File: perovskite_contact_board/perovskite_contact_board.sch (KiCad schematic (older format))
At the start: 14 parts, among them J1 Conn_02x03_Counter_Clockwise, J2 Conn_02x03_Counter_Clockwise, J3 Conn_02x03_Counter_Clockwise, J4 Conn_02x03_Counter_Clockwise, J5 Conn_02x03_Counter_Clockwise, J6 Conn_02x03_Counter_Clockwise, U1 Perovskite_CP_6_Cell, U2 Perovskite_CP_6_Cell, U3 Perovskite_CP_6_Cell, U4 MCP9808_MSOP, U5 MCP9808_MSOP, U6 MCP9808_MSOP

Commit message: pushing changes from Monday meeting
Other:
- moved on the sheet: R1, R4, U1, U2, U3, U4, U5, U6

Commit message: Switched to 0603 package, no longer castillated holes used for the mcp9804, all traces on back layer
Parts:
- removed J1, J2, J3, J4, J5, J6: Conn_02x03_Counter_Clockwise, Connector_PinHeader_2.54mm:PinHeader_2x03_P2.54mm_Vertical_SMD, symbol Connector_Generic:Conn_02x03_Counter_Clockwise
- added J1, J2, J3, J4, J5, J6: Conn_01x08, Connector_PinSocket_2.54mm:PinSocket_1x08_P2.54mm_Vertical_SMD_Pin1Left, symbol Connector_Generic:Conn_01x08
- R1, R4: footprint Resistor_SMD:R_0805_2012Metric -> Resistor_SMD:R_0603_1608Metric
- U4, U5, U6: footprint MCP9804Castillated:CastillatedMCP9804 -> MCP9804_Custom:MCP9804_With_Hole
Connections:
- net labels added: +5V, ALERT1, ALERT2, ALERT3, CELL_1, CELL_10, CELL_11, CELL_12, CELL_13, CELL_14, CELL_15, CELL_16, CELL_17, CELL_18, CELL_2, CELL_3, CELL_4, CELL_5, CELL_6, CELL_7, CELL_8, CELL_9
- net labels removed: 1, 10, 11, 12, 13, 14, 15, 16, 17, 18, 2, 3, 4, 5, 6, 7, 8, 9, Alert1, Alert2, Alert3, Vdd
- wire segments 15 -> 73
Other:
- note added: "Perovskite 1"
- note added: "Perovskite 2"
- note added: "Perovskite 3"
- note added: "Pull Up"
- moved on the sheet: R1, R4, U1, U2, U3, U4, U5, U6

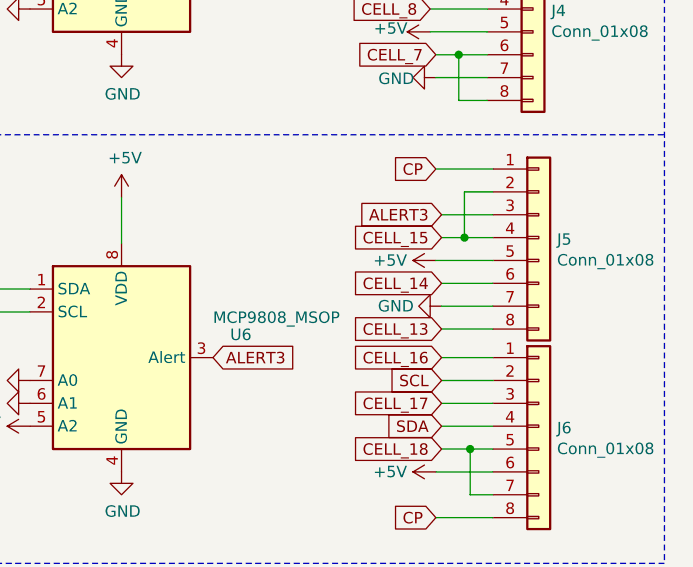
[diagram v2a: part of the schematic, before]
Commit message: Contact board update with 2.54 spacing
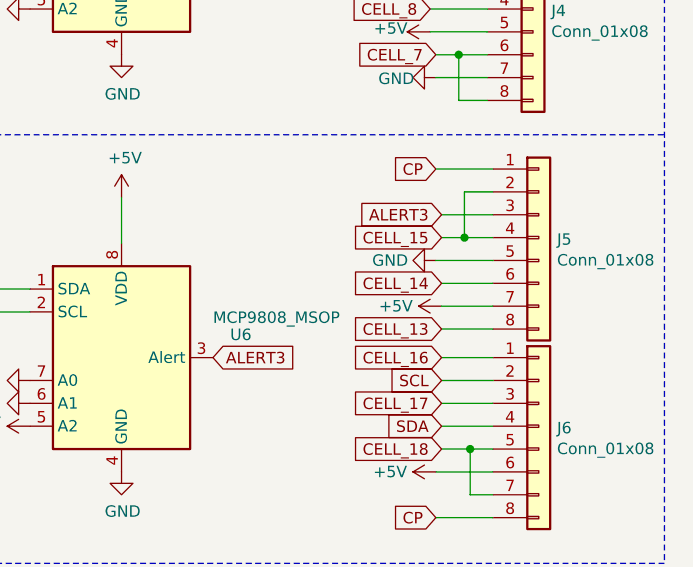
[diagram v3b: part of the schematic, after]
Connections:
- net +5V: now also J5.7 (Pin_7); no longer J5.5 (Pin_5)
- net GND: now also J5.5 (Pin_5); no longer J5.7 (Pin_7)
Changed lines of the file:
@@
 L power:GND #PWR0121
 U 1 1 636DD992
-P 7125 5175
-F 0 "#PWR0121" H 7125 4925 50  0001 C CNN
-F 1 "GND" V 7125 4975 50  0000 C CNN
-F 2 "" H 7125 5175 50  0001 C CNN
-F 3 "" H 7125 5175 50  0001 C CNN
-	1    7125 5175
+P 7100 4975
+F 0 "#PWR0121" H 7100 4725 50  0001 C CNN
+F 1 "GND" V 7100 4775 50  0000 C CNN
+F 2 "" H 7100 4975 50  0001 C CNN
+F 3 "" H 7100 4975 50  0001 C CNN
+	1    7100 4975
 	0    1    1    0
 $EndComp
@@
 L power:+5V #PWR0123
 U 1 1 6375EA4D
-P 7100 4975
-F 0 "#PWR0123" H 7100 4825 50  0001 C CNN
-F 1 "+5V" V 7100 5175 50  0000 C CNN
-F 2 "" H 7100 4975 50  0001 C CNN
-F 3 "" H 7100 4975 50  0001 C CNN
-	1    7100 4975
+P 7125 5175
+F 0 "#PWR0123" H 7125 5025 50  0001 C CNN
+F 1 "+5V" V 7125 5375 50  0000 C CNN
+F 2 "" H 7125 5175 50  0001 C CNN
+F 3 "" H 7125 5175 50  0001 C CNN
+	1    7125 5175
 	0    -1   1    0
 $EndComp

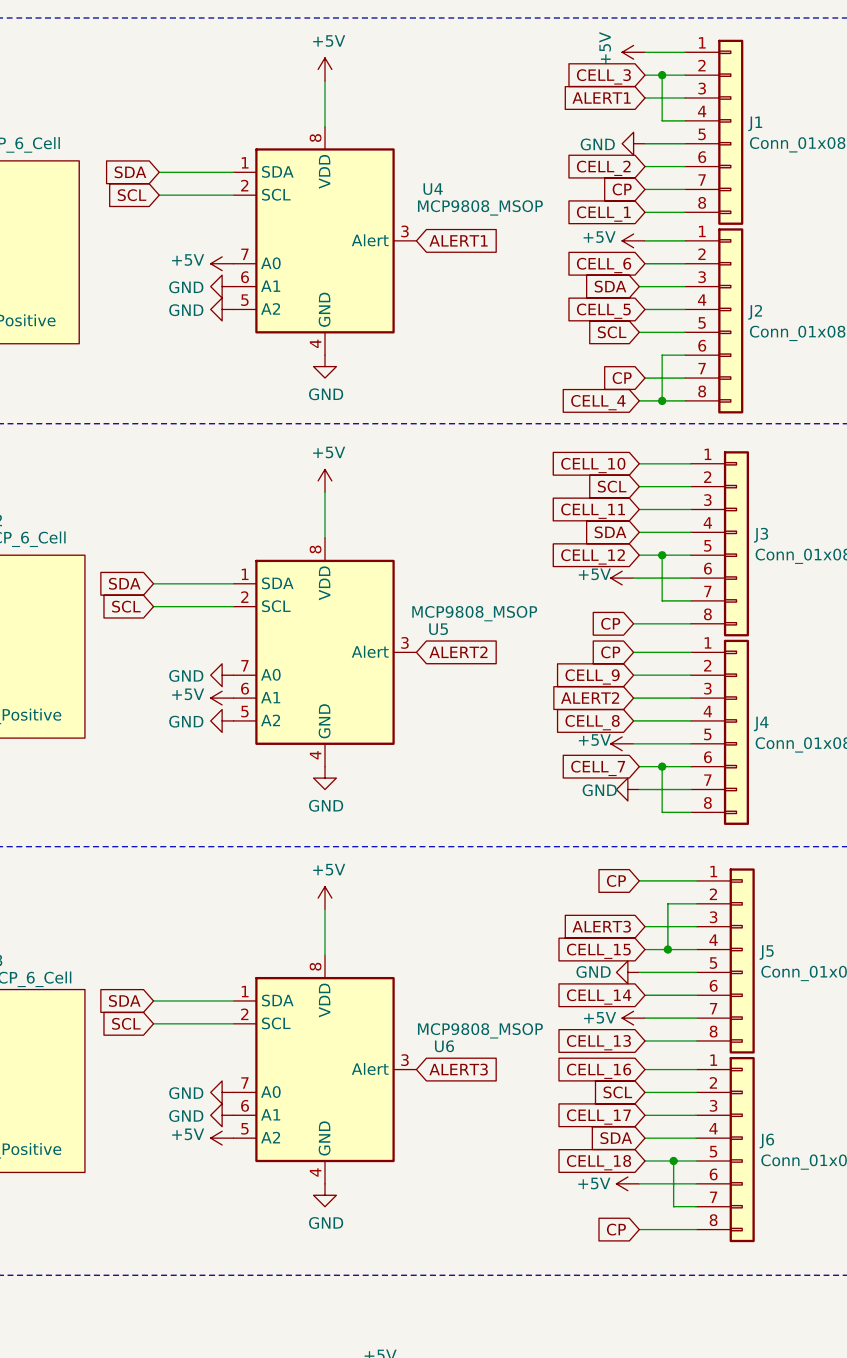
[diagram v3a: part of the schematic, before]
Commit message: moved headers to fit connection to routing board and switch symbols to proper form
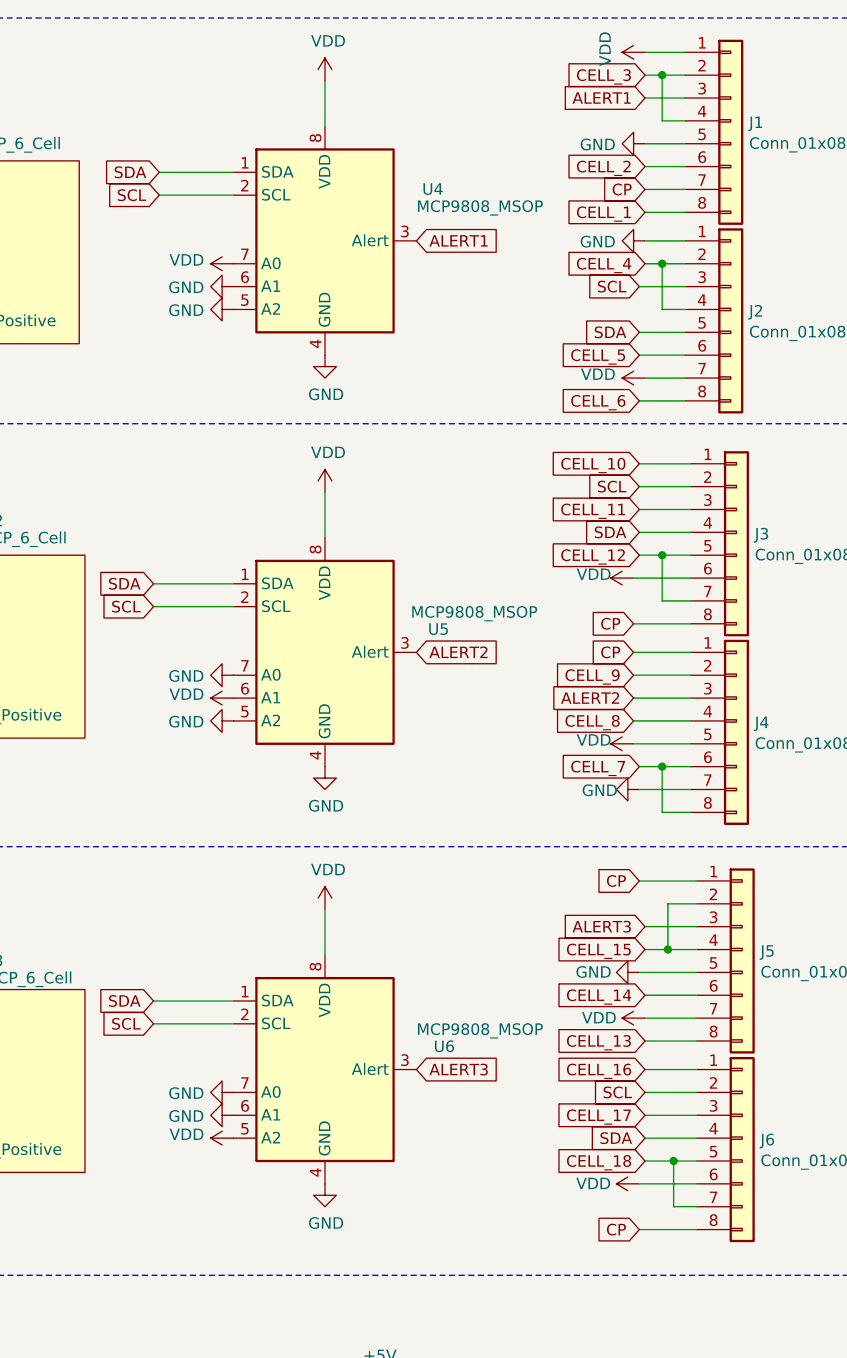
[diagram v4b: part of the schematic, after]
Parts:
- J2: footprint Connector_PinSocket_2.54mm:PinSocket_1x08_P2.54mm_Vertical_SMD_Pin1Left -> Connector_PinSocket_2.54mm:PinSocket_1x08_P2.54mm_Vertical_SMD_Pin1Right
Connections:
- net +5V: no longer J1.1 (Pin_1), J2.1 (Pin_1), J3.6 (Pin_6), J4.5 (Pin_5), J5.7 (Pin_7), J6.6 (Pin_6), U4.7 (A0), U4.8 (VDD), U5.6 (A1), U5.8 (VDD), U6.5 (A2), U6.8 (VDD)
- net CELL_4: now also J2.2 (Pin_2), J2.4 (Pin_4); no longer J2.6 (Pin_6), J2.8 (Pin_8)
- net CELL_5: now also J2.6 (Pin_6); no longer J2.4 (Pin_4)
- net CELL_6: now also J2.8 (Pin_8); no longer J2.2 (Pin_2)
- net CP: no longer J2.7 (Pin_7)
- net GND: now also J2.1 (Pin_1)
- net SCL: now also J2.3 (Pin_3); no longer J2.5 (Pin_5)
- net SDA: now also J2.5 (Pin_5); no longer J2.3 (Pin_3)
- new net VDD: J1.1 (Pin_1), J2.7 (Pin_7), J3.6 (Pin_6), J4.5 (Pin_5), J5.7 (Pin_7), J6.6 (Pin_6), U4.7 (A0), U4.8 (VDD), U5.6 (A1), U5.8 (VDD), U6.5 (A2), U6.8 (VDD)
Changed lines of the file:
@@
 Text GLabel 7125 1050 0    50   Input ~ 0
 CELL_3
+Text GLabel 7125 1875 0    50   Input ~ 0
+CELL_4
+Text GLabel 7100 2275 0    50   Input ~ 0
+CELL_5
 Text GLabel 7100 2475 0    50   Input ~ 0
-CELL_4
-Text GLabel 7125 2075 0    50   Input ~ 0
-CELL_5
-Text GLabel 7125 1875 0    50   Input ~ 0
 CELL_6
 Text GLabel 7100 4075 0    50   Input ~ 0
@@
 Text GLabel 7100 2850 0    50   Input ~ 0
 SCL
+Text GLabel 7100 2175 0    50   Input ~ 0
+SDA
 Text GLabel 7100 1975 0    50   Input ~ 0
-SDA
-Text GLabel 7100 2175 0    50   Input ~ 0
 SCL
 $Comp
@@
 F 0 "J2" H 7580 2067 50  0000 L CNN
 F 1 "Conn_01x08" H 7580 1976 50  0000 L CNN
-F 2 "Connector_PinSocket_2.54mm:PinSocket_1x08_P2.54mm_Vertical_SMD_Pin1Left" H 7500 2075 50  0001 C CNN
+F 2 "Connector_PinSocket_2.54mm:PinSocket_1x08_P2.54mm_Vertical_SMD_Pin1Right" H 7500 2075 50  0001 C CNN
 F 3 "~" H 7500 2075 50  0001 C CNN
 	1    7500 2075
@@
 $EndComp
 Wire Wire Line
-	7300 2475 7200 2475
-Wire Wire Line
-	7300 2275 7200 2275
-Wire Wire Line
-	7200 2275 7200 2475
-Connection ~ 7200 2475
-Wire Wire Line
-	7200 2475 7100 2475
-Text GLabel 7125 2375 0    50   Input ~ 0
-CP
-Wire Wire Line
 	7300 2375 7125 2375
 Wire Wire Line
 	7300 1150 7125 1150
 $Comp
-L power:+5V #PWR0101
+L power:VDD #PWR0101
 U 1 1 636CF85F
 P 5725 1075
 F 0 "#PWR0101" H 5725 925 50  0001 C CNN
-F 1 "+5V" H 5740 1248 50  0000 C CNN
+F 1 "VDD" H 5740 1248 50  0000 C CNN
 F 2 "" H 5725 1075 50  0001 C CNN
 F 3 "" H 5725 1075 50  0001 C CNN
@@
 $EndComp
 $Comp
-L power:+5V #PWR0102
+L power:VDD #PWR0102
 U 1 1 636D0D79
 P 5325 1875
 F 0 "#PWR0102" H 5325 1725 50  0001 C CNN
-F 1 "+5V" V 5340 2003 50  0000 L CNN
+F 1 "VDD" V 5340 2003 50  0000 L CNN
 F 2 "" H 5325 1875 50  0001 C CNN
 F 3 "" H 5325 1875 50  0001 C CNN
@@
 $EndComp
 $Comp
-L power:+5V #PWR0103
+L power:VDD #PWR0103
 U 1 1 636D2A3F
 P 5325 3775
 F 0 "#PWR0103" H 5325 3625 50  0001 C CNN
-F 1 "+5V" V 5340 3903 50  0000 L CNN
+F 1 "VDD" V 5340 3903 50  0000 L CNN
 F 2 "" H 5325 3775 50  0001 C CNN
 F 3 "" H 5325 3775 50  0001 C CNN
@@
 $EndComp
 $Comp
-L power:+5V #PWR0104
+L power:VDD #PWR0104
 U 1 1 636D451D
 P 5325 5700
 F 0 "#PWR0104" H 5325 5550 50  0001 C CNN
-F 1 "+5V" V 5340 5828 50  0000 L CNN
+F 1 "VDD" V 5340 5828 50  0000 L CNN
 F 2 "" H 5325 5700 50  0001 C CNN
 F 3 "" H 5325 5700 50  0001 C CNN
@@
 $EndComp
 $Comp
-L power:+5V #PWR0105
+L power:VDD #PWR0105
 U 1 1 636D5369
 P 5725 4700
 F 0 "#PWR0105" H 5725 4550 50  0001 C CNN
-F 1 "+5V" H 5740 4873 50  0000 C CNN
+F 1 "VDD" H 5740 4873 50  0000 C CNN
 F 2 "" H 5725 4700 50  0001 C CNN
 F 3 "" H 5725 4700 50  0001 C CNN
@@
 $EndComp
 $Comp
-L power:+5V #PWR0106
+L power:VDD #PWR0106
 U 1 1 636D60D1
 P 7100 5900
 F 0 "#PWR0106" H 7100 5750 50  0001 C CNN
-F 1 "+5V" V 7100 6100 50  0000 C CNN
+F 1 "VDD" V 7100 6100 50  0000 C CNN
 F 2 "" H 7100 5900 50  0001 C CNN
 F 3 "" H 7100 5900 50  0001 C CNN
@@
 $EndComp
 $Comp
-L power:+5V #PWR0109
+L power:VDD #PWR0109
 U 1 1 636D8999
 P 5725 2875
 F 0 "#PWR0109" H 5725 2725 50  0001 C CNN
-F 1 "+5V" H 5740 3048 50  0000 C CNN
+F 1 "VDD" H 5740 3048 50  0000 C CNN
 F 2 "" H 5725 2875 50  0001 C CNN
 F 3 "" H 5725 2875 50  0001 C CNN
@@
 $EndComp
 Wire Wire Line
-	7300 1875 7125 1875
-Wire Wire Line
-	7300 2075 7125 2075
+	7300 1875 7200 1875
 Wire Wire Line
 	7300 1650 7125 1650
@@
 	7125 1350 7300 1350
 $Comp
-L power:+5V #PWR0122
+L power:VDD #PWR0122
 U 1 1 636E8046
-P 7125 1775
-F 0 "#PWR0122" H 7125 1625 50  0001 C CNN
-F 1 "+5V" V 7140 1903 50  0000 L CNN
-F 2 "" H 7125 1775 50  0001 C CNN
-F 3 "" H 7125 1775 50  0001 C CNN
-	1    7125 1775
+P 7125 2375
+F 0 "#PWR0122" H 7125 2225 50  0001 C CNN
+F 1 "VDD" V 7140 2503 50  0000 L CNN
+F 2 "" H 7125 2375 50  0001 C CNN
+F 3 "" H 7125 2375 50  0001 C CNN
+	1    7125 2375
 	0    -1   -1   0
 $EndComp
@@
 	7300 1250 7200 1250
 $Comp
-L power:+5V #PWR0108
+L power:VDD #PWR0108
 U 1 1 636D7986
 P 7125 950
 F 0 "#PWR0108" H 7125 800 50  0001 C CNN
-F 1 "+5V" H 7140 1123 50  0000 C CNN
+F 1 "VDD" H 7140 1123 50  0000 C CNN
 F 2 "" H 7125 950 50  0001 C CNN
 F 3 "" H 7125 950 50  0001 C CNN
@@
 	7100 3050 7325 3050
 $Comp
-L power:+5V #PWR0124
+L power:VDD #PWR0124
 U 1 1 637067F2
 P 7075 3250
 F 0 "#PWR0124" H 7075 3100 50  0001 C CNN
-F 1 "+5V" V 7090 3423 50  0000 C CNN
+F 1 "VDD" V 7090 3423 50  0000 C CNN
 F 2 "" H 7075 3250 50  0001 C CNN
 F 3 "" H 7075 3250 50  0001 C CNN
@@
 	7075 3775 7325 3775
 $Comp
-L power:+5V #PWR0107
+L power:VDD #PWR0107
 U 1 1 6371D2C2
 P 7075 3975
 F 0 "#PWR0107" H 7075 3825 50  0001 C CNN
-F 1 "+5V" V 7090 4148 50  0000 C CNN
+F 1 "VDD" V 7090 4148 50  0000 C CNN
 F 2 "" H 7075 3975 50  0001 C CNN
 F 3 "" H 7075 3975 50  0001 C CNN
@@
 	7125 5175 7350 5175
 $Comp
-L power:+5V #PWR0123
+L power:VDD #PWR0123
 U 1 1 6375EA4D
 P 7125 5175
 F 0 "#PWR0123" H 7125 5025 50  0001 C CNN
-F 1 "+5V" V 7125 5375 50  0000 C CNN
+F 1 "VDD" V 7125 5375 50  0000 C CNN
 F 2 "" H 7125 5175 50  0001 C CNN
 F 3 "" H 7125 5175 50  0001 C CNN
@@
 	5000 1575 5325 1575
 $Comp
-L power:+5V #PWR?
+L power:+5V #PWR0125
 U 1 1 63736E10
 P 5950 6825
-F 0 "#PWR?" H 5950 6675 50  0001 C CNN
+F 0 "#PWR0125" H 5950 6675 50  0001 C CNN
 F 1 "+5V" H 5965 6998 50  0000 C CNN
 F 2 "" H 5950 6825 50  0001 C CNN
@@
 Text Notes 4500 7125 0    197  ~ 0
 Pull Up
+Wire Wire Line
+	7100 2475 7300 2475
+Wire Wire Line
+	7300 2075 7200 2075
+Wire Wire Line
+	7200 2075 7200 1875
+Connection ~ 7200 1875
+Wire Wire Line
+	7200 1875 7125 1875
+Wire Wire Line
+	7300 2275 7100 2275
+$Comp
+L power:GND #PWR?
+U 1 1 6378F3C5
+P 7125 1775
+F 0 "#PWR?" H 7125 1525 50  0001 C CNN
+F 1 "GND" V 7130 1647 50  0000 R CNN
+F 2 "" H 7125 1775 50  0001 C CNN
+F 3 "" H 7125 1775 50  0001 C CNN
+	1    7125 1775
+	0    1    1    0
+$EndComp
 $EndSCHEMATC

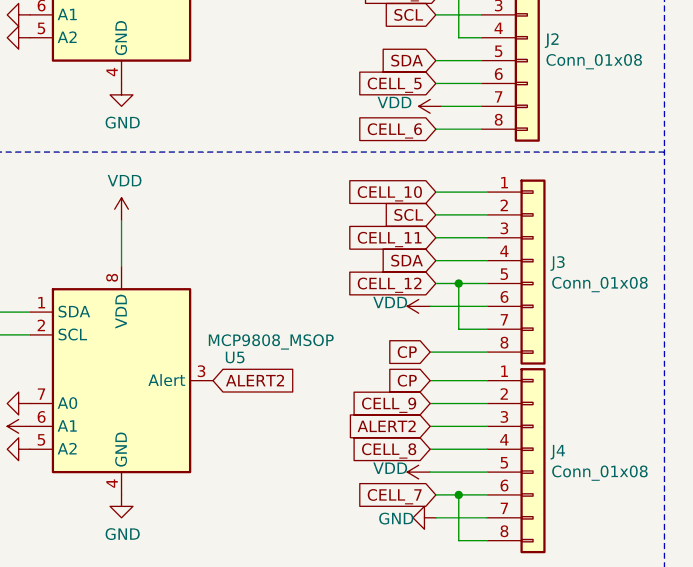
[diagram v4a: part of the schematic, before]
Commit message: new headers added and spacing fixed to allow for 26 pin connector
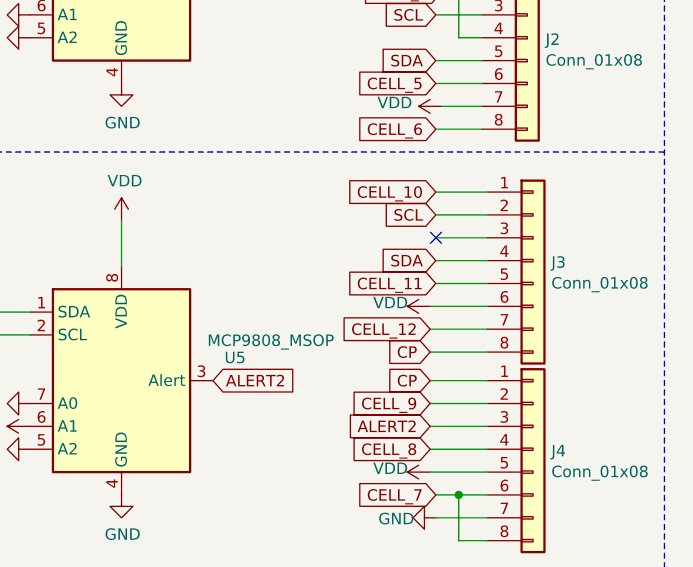
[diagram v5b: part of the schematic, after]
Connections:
- net CELL_11: now also J3.5 (Pin_5); no longer J3.3 (Pin_3)
- net CELL_12: no longer J3.5 (Pin_5)
- no-connect marks 0 -> 1
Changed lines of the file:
@@
 Text GLabel 7100 2750 0    50   Input ~ 0
 CELL_10
-Text GLabel 7100 2950 0    50   Input ~ 0
+Text GLabel 7100 3150 0    50   Input ~ 0
 CELL_11
-Text GLabel 7100 3150 0    50   Input ~ 0
+Text GLabel 7075 3350 0    50   Input ~ 0
 CELL_12
 Text GLabel 7125 5275 0    50   Input ~ 0
@@
 Wire Wire Line
 	7325 3875 7075 3875
-Wire Wire Line
-	7325 3150 7200 3150
-Wire Wire Line
-	7325 3350 7200 3350
-Wire Wire Line
-	7200 3350 7200 3150
-Connection ~ 7200 3150
-Wire Wire Line
-	7200 3150 7100 3150
 Wire Wire Line
 	7325 2750 7100 2750
@@
 	0    1    1    0
 $EndComp
+Wire Wire Line
+	7100 3150 7325 3150
+Wire Wire Line
+	7075 3350 7325 3350
+NoConn ~ 7100 2950
 $EndSCHEMATC
